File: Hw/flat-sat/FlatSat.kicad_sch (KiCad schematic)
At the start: 81 parts, among them J1 Antenna, J2 Antenna, P1 USB_C_Plug_USB2.0, SW1 SW, SW2 SW, U1 AP2112K-3.3, U10 LIS2DH, U2 0900FM15D0039, U3 PE42421, U4 SX1262IMLTRT, U5 W25Q16JV, U6 0900FM15D0039, U7 PE42421, U8 SX1262IMLTRT, U9 RP2040, Y1 32Mhz, Y2 32Mhz, Y3 12MHz

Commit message: feat(Hw):Update_sch
Pending review
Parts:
- removed SW1, SW2: SW, CatSniffer:TS1088R02026, symbol CatSniffer-rescue:SW_Push-Switch-CatStick-rescue-CatSniffer-rescue
- added J3: Serial, symbol Connector:Conn_01x04_Pin
- added J4: SWD, symbol Connector:Conn_01x04_Pin
- U1: value AP2112K-3.3 -> TLV75733PDBVR; LCSC# (none) -> C485517; Mouser# 865-XC6210B332MR-G -> (none); manf# XC6210B332MR-G -> TLV75733PDBVR; provedor Mouser -> LCSC
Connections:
- net CIPO is gone; now on net R0_CIPO: U9.27 (GPIO16)
- net COPI is gone; now on net R0_COPI: U9.30 (GPIO19)
- net NSS is gone; now on net R0_NSS: U9.28 (GPIO17)
- net R0_DIO22 is gone; now on net DIO2: JP1.1 (A)
- net R1_DIO22 is gone; now on net DIO23: JP2.1 (A)
- net SCK is gone; now on net R0_SCK: U9.29 (GPIO18)
- net +3V3: now also J3.4 (Pin_4), J4.4 (Pin_4)
- net GND: now also J3.1 (Pin_1), J4.1 (Pin_1)
- net LED1: now also U9.16 (GPIO13); no longer U9.40 (GPIO28_ADC2)
- net LED2: now also U9.17 (GPIO14); no longer U9.39 (GPIO27_ADC1)
- net LED3: now also U9.18 (GPIO15); no longer U9.38 (GPIO26_ADC0)
- net R0_ANT_SW: now also U9.40 (GPIO28_ADC2)
- net R0_BUSY: now also U9.9 (GPIO7)
- net R0_DIO1: now also U9.5 (GPIO3)
- net R0_DIO2: now also U9.6 (GPIO4)
- net R0_DIO3: now also U9.7 (GPIO5)
- net R0_RST: now also U9.8 (GPIO6)
- net R1_ANT_SW: now also U9.41 (GPIO29_ADC3)
- net R1_BUSY: now also U9.15 (GPIO12)
- net R1_CIPO: now also U9.36 (GPIO24)
- net R1_COPI: now also U9.39 (GPIO27_ADC1)
- net R1_DIO1: now also U9.11 (GPIO8)
- net R1_DIO2: now also U9.12 (GPIO9)
- net R1_DIO3: now also U9.13 (GPIO10)
- net R1_NSS: now also U9.37 (GPIO25)
- net R1_RST: now also U9.14 (GPIO11)
- net R1_SCK: now also U9.38 (GPIO26_ADC0)
- net SWCLK: now also J4.3 (Pin_3)
- net SCL: now reaches U10.1 (SCL/SPC)
- net SCL: now also U9.32 (GPIO21)
- net SDA: now reaches U10.2 (SDA/SDI)
- net SDA: now also U9.31 (GPIO20)
- net INT1: now reaches U10.6 (INT1)
- net INT1: now also U9.34 (GPIO22)
- net TXD: now reaches U9.2 (GPIO0)
- net TXD: now also J3.3 (Pin_3)
- net RXD: now reaches U9.3 (GPIO1)
- net RXD: now also J3.2 (Pin_2)
- net DIO23: now reaches U9.35 (GPIO23)
- net DIO2: now reaches U9.4 (GPIO2)
- new net SWDIO: J4.2 (Pin_2)
- no-connect marks 3 -> 5
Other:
- moved on the sheet: BOOT1, C6, C7, JP1, JP2, R1, R2, RESET1, U1, U10

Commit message: fet(Hw):Init_floorplan_Update_LCSC#
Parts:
- removed D2, D3: LED, LED_SMD:LED_0603_1608Metric_Pad1.05x0.95mm_HandSolder, symbol CatSniffer-rescue:LED_Small-Device-CatStick-rescue-CatSniffer-rescue
- removed R11, R12: 330, Resistor_SMD:R_0603_1608Metric, symbol CatSniffer-rescue:R_Small-Device-CatStick-rescue-CatSniffer-rescue
- added Button1, Button2: SW, CatSniffer:TS1088R02026, symbol CatSniffer-rescue:SW_Push-Switch-CatStick-rescue-CatSniffer-rescue
- added C37: 0.1uF, Capacitor_SMD:C_0402_1005Metric, symbol Device:C_Small
- added R11, R12: 10k, Resistor_SMD:R_0402_1005Metric, symbol Device:R_Small
- BOOT1, RESET1: manf# TS-1088R-02526 -> (none)
- C1, C14, C18, C19, C5, C7, C8: footprint Capacitor_SMD:C_0603_1608Metric -> Capacitor_SMD:C_0402_1005Metric; LCSC# C14663 -> C56392; manf# CC0603KRX7R9BB104 -> (none)
- C10, C12, C21, C23: footprint Capacitor_SMD:C_0603_1608Metric -> Capacitor_SMD:C_0402_1005Metric; LCSC# C1588 -> C710873; manf# CL10B102KB8NNNC -> (none)
- C11, C22: footprint Capacitor_SMD:C_0603_1608Metric -> Capacitor_SMD:C_0402_1005Metric; LCSC# C170149 -> C47339; manf# CL10A474KB8NNNC -> (none)
- C13, C24, C25, C27, C28, C32, C33, C34, C35, C36: LCSC# (none) -> C56392; manf# MSAST105SB7104KFNB25 -> (none)
- C15, C2: footprint Capacitor_SMD:C_0603_1608Metric -> Capacitor_SMD:C_0402_1005Metric; LCSC# C14858 -> C541374; manf# CL10C101JB8NNNC -> (none)
- C16, C17, C3, C4: footprint Capacitor_SMD:C_0603_1608Metric -> Capacitor_SMD:C_0402_1005Metric; LCSC# C162225 -> C1565; manf# GRM1885C1H3R3CA01D -> (none)
- C20, C9: footprint Capacitor_SMD:C_0603_1608Metric -> Capacitor_SMD:C_0402_1005Metric; LCSC# C519486 -> C437519; manf# CC0603FRNPO9BN470 -> (none)
- C26, C31: LCSC# (none) -> C52923; manf# MSRLJ103SB5105MFNA01 -> (none)
- C29, C30: LCSC# (none) -> C424826; manf# GJM1555C1H270FB01D -> (none)
- C6: footprint Capacitor_SMD:C_0603_1608Metric -> Capacitor_SMD:C_0402_1005Metric; LCSC# C108343 -> C52923; manf# 0603F105M500NT -> (none)
- D1: manf# CL10C120JB81PNC -> (none)
- F1: value 0.5A -> 0.75A; footprint Fuse:Fuse_0805_2012Metric_Pad1.15x1.40mm_HandSolder -> Fuse:Fuse_0603_1608Metric_Pad1.05x0.95mm_HandSolder; LCSC# (none) -> C182438; manf# MFU0805FF00500P100 -> (none)
- J1, J2: footprint bast-wan:SMA_EDGE -> FlatSat:SMA_EDGE; manf# KH-SMA-KE8-G -> (none)
- J3, J4: footprint (none) -> Connector_PinHeader_2.54mm:PinHeader_1x04_P2.54mm_Vertical
- L1, L4: manf# VHF160808H9N1JT -> (none)
- L2, L5: manf# SCHF160808H47NJT -> (none)
- L3, L6: manf# SDFL1608T150KTF -> (none)
- P1: footprint Connectors:C393939 -> FlatSat:C393939; manf# KH-TYPE-C-16P -> (none)
- R1, R2: footprint Resistor_SMD:R_0603_1608Metric -> Resistor_SMD:R_0402_1005Metric; LCSC# C319561 -> C25905; manf# AR03DTCX5101 -> (none)
- R10, R8: LCSC# (none) -> C25100; manf# ESR01MZPF27R0 -> (none)
- R13: LCSC# (none) -> C11702; manf# MCS0402MD1001DE000 -> (none)
- R3, R4, R6, R7: footprint Resistor_SMD:R_0603_1608Metric -> Resistor_SMD:R_0402_1005Metric; LCSC# C700506 -> C25076; manf# RT0603DRD07100RL -> (none)
- R5: LCSC# (none) -> C25531; manf# MCS04020D1002BE000 -> (none)
- R9: manf# AR03BTB3300 -> (none)
- U1: manf# TLV75733PDBVR -> (none)
- U2, U6: footprint CatSniffer:0900FM15D0039E -> FlatSat:0900FM15D0039E
- U3, U7: LCSC# - -> C470893
- U4, U8: LCSC# (none) -> C191341
- U5: footprint CatSniffer:W25Q16JVUUIQ -> Package_SON:Winbond_USON-8-2EP_3x4mm_P0.8mm_EP0.2x0.8mm; LCSC# (none) -> C571259
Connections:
- net +3V3: now also C37.1, R11.1, R12.1
- net GND: now also Button1.2, Button2.2, C37.2
- net LED1: now also D1.2 (A)
- net SCL: now also R12.2
- net SDA: now also R11.2
- net LED2 renamed Butt_1
- net Butt_1: now also Button1.1
- net LED3 renamed Butt_2
- net Butt_2: now also Button2.1; no longer D1.2 (A)
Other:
- moved on the sheet: U10

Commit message: feat(Hw):Update_Pcb_And
Pending_some_pins
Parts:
- BOOT1, Button1, Button2, RESET1: footprint CatSniffer:TS1088R02026 -> Button_Switch_SMD:SW_SPST_TL3342
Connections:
- net SWD is gone; now on net SWDIO: U9.25 (SWD)
- net Butt_1: now also U9.15 (GPIO12); no longer U9.17 (GPIO14)
- net Butt_2: now also U9.16 (GPIO13); no longer U9.18 (GPIO15)
- net GND: now also U4.25 (EXP), U8.25 (EXP)
- net LED1: now also U9.18 (GPIO15); no longer U9.16 (GPIO13)
- net R0_BUSY: now also U9.38 (GPIO26_ADC0); no longer U9.9 (GPIO7)
- net R0_DIO2: now also U9.36 (GPIO24); no longer U9.6 (GPIO4)
- net R0_DIO3: now also U9.37 (GPIO25); no longer U9.7 (GPIO5)
- net R0_RST: now also U9.39 (GPIO27_ADC1); no longer U9.8 (GPIO6)
- net R1_BUSY: now also U9.17 (GPIO14); no longer U9.15 (GPIO12)
- net R1_CIPO: now also U9.6 (GPIO4); no longer U9.36 (GPIO24)
- net R1_COPI: now also U9.9 (GPIO7); no longer U9.39 (GPIO27_ADC1)
- net R1_NSS: now also U9.7 (GPIO5); no longer U9.37 (GPIO25)
- net R1_SCK: now also U9.8 (GPIO6); no longer U9.38 (GPIO26_ADC0)
- net RXD: now also J3.3 (Pin_3); no longer J3.2 (Pin_2)
- net TXD: now also J3.2 (Pin_2); no longer J3.3 (Pin_3)
- net RD+: now reaches R8.2, U9.47 (USB_DP)
- net RD-: now reaches R10.2, U9.46 (USB_DM)
- no-connect marks 5 -> 3
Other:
- moved on the sheet: C1, C11, C19, C20, C22, C8, C9, L2, L3, L5, L6, U4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

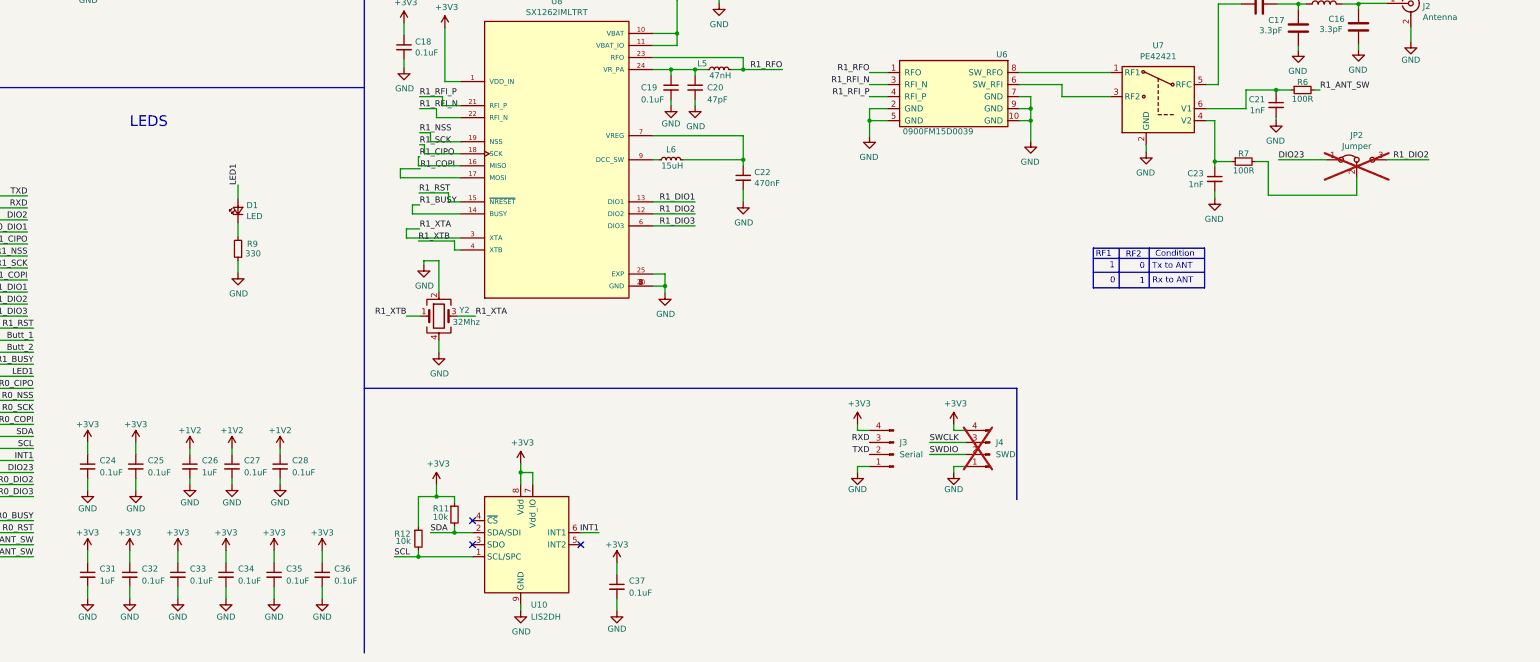
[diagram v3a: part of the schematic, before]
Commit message: feat(Hw):Mounting_Holes_Added
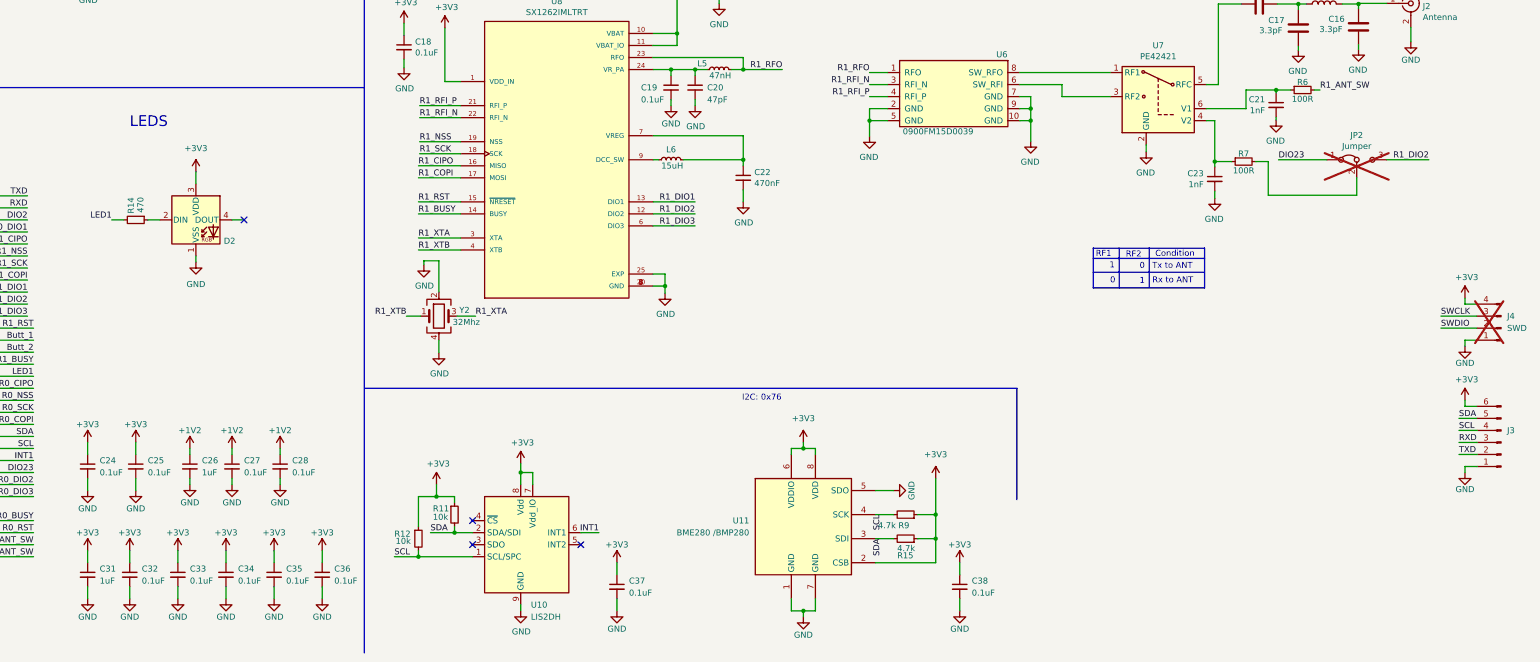
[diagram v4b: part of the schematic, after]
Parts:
- removed D1: LED, LED_SMD:LED_0603_1608Metric_Pad1.05x0.95mm_HandSolder, symbol CatSniffer-rescue:LED_Small-Device-CatStick-rescue-CatSniffer-rescue
- removed J3: Serial, Connector_PinHeader_2.54mm:PinHeader_1x04_P2.54mm_Vertical, symbol Connector:Conn_01x04_Pin
- removed R9: 330, Resistor_SMD:R_0603_1608Metric, symbol CatSniffer-rescue:R_Small-Device-CatStick-rescue-CatSniffer-rescue
- added C38: 0.1uF, Capacitor_SMD:C_0402_1005Metric, symbol Device:C_Small
- added D2: SK6812MINI, Library:SK6812MINI-HS, symbol LED:SK6812MINI
- added J3: periphs, Connector_PinHeader_2.54mm:PinHeader_1x06_P2.54mm_Vertical, symbol Connector:Conn_01x06_Pin
- added R14: 470, Resistor_SMD:R_0402_1005Metric, symbol CatSniffer-rescue:R_Small-Device-CatStick-rescue-CatSniffer-rescue
- added R15, R9: 4.7k, Resistor_SMD:R_0402_1005Metric, symbol Device:R_Small
- added U11: BME280 /BMP280, Package_LGA:Bosch_LGA-8_2.5x2.5mm_P0.65mm_ClockwisePinNumbering, symbol Sensor:BME280
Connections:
- net +3V3: now also C38.1, D2.3 (VDD), J3.6 (Pin_6), R15.1, R9.1, U11.2 (CSB), U11.6 (VDDIO), U11.8 (VDD)
- net GND: now also C38.2, D2.1 (VSS), J3.1 (Pin_1), U11.1 (GND), U11.5 (SDO), U11.7 (GND)
- net LED1: now also R14.2
- net RXD: now also J3.3 (Pin_3)
- net SCL: now also J3.4 (Pin_4), R9.2, U11.4 (SCK)
- net SDA: now also J3.5 (Pin_5), R15.2, U11.3 (SDI)
- net TXD: now also J3.2 (Pin_2)
- new net: D2.2 (DIN), R14.1
- no-connect marks 3 -> 4
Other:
- note added: "I2C: 0x76"
- moved on the sheet: J4

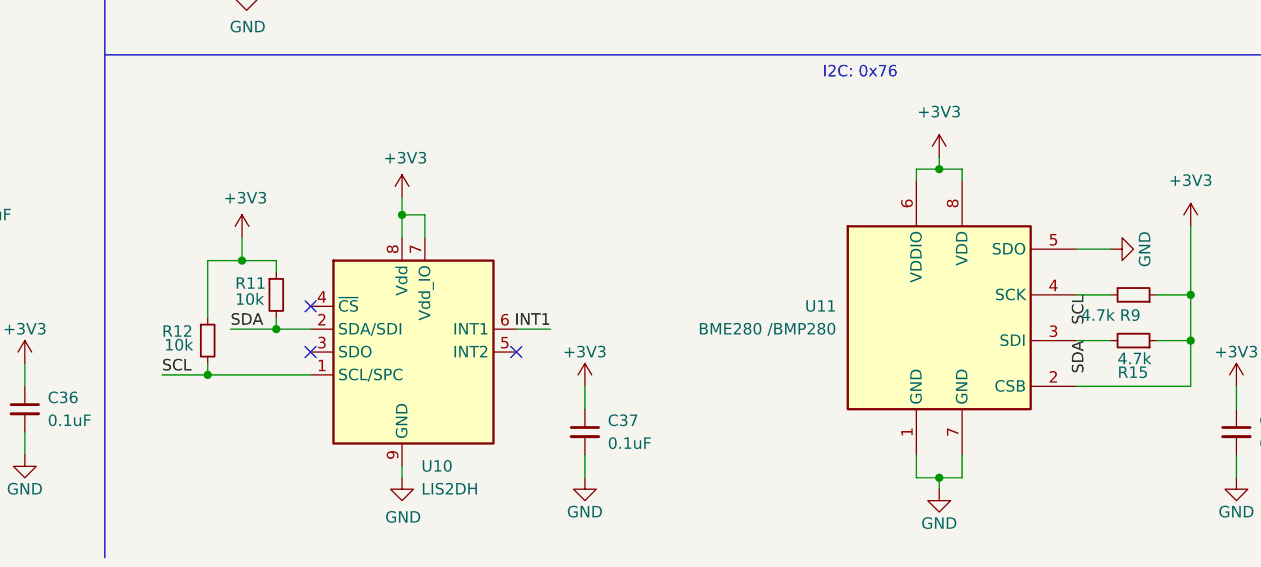
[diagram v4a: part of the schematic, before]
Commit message: feat(Hw):Update_PCB_Change_Buttons
Pending_Check_LIS2DH
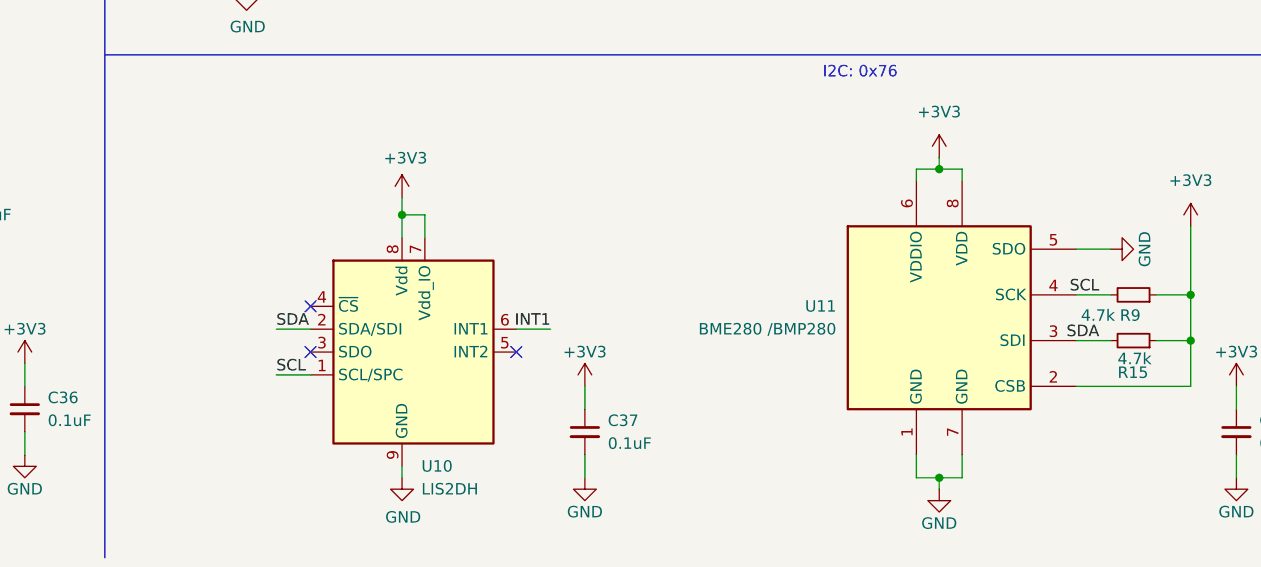
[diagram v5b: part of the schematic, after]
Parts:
- removed R11, R12: 10k, Resistor_SMD:R_0402_1005Metric, symbol Device:R_Small
- BOOT1, Button1, Button2, RESET1: footprint Button_Switch_SMD:SW_SPST_TL3342 -> FlatSat:TS1088R02026
- U10: LCSC# C110926 -> C155670

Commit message: feat(Hw):Update_BoM
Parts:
- C10, C12, C21, C23: LCSC# C710873 -> C335530
- C13, C24, C25, C27, C28, C32, C33, C34, C35, C36, C37, C38: Mouser# 963-MSAST105SB7104KF -> (none)
- C26, C31: Mouser# 963-MSRLJ103SB5105MF -> (none)
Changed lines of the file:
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@@
 			)
 		)
-		(property "LCSC#" "C710873 "
+		(property "LCSC#" "C335530"
 			(at 352.298 63.754 0)
 			(effects
@@
 			)
 		)
-		(property "Mouser#" "963-MSRLJ103SB5105MF"
+		(property "Mouser#" ""
 			(at 137.16 228.6 0)
 			(effects
@@
 			)
 		)
-		(property "Mouser#" "963-MSAST105SB7104KF"
+		(property "Mouser#" ""
 			(at 125.73 228.6 0)
 			(effects
@@
 			)
 		)
-		(property "Mouser#" "963-MSAST105SB7104KF"
+		(property "Mouser#" ""
 			(at 134.62 251.46 0)
 			(effects
@@
 			)
 		)
-		(property "Mouser#" "963-MSRLJ103SB5105MF"
+		(property "Mouser#" ""
 			(at 115.57 251.46 0)
 			(effects
@@
 			)
 		)
-		(property "LCSC#" "C710873 "
+		(property "LCSC#" "C335530"
 			(at 353.568 167.894 0)
 			(effects
@@
 			)
 		)
-		(property "LCSC#" "C710873 "
+		(property "LCSC#" "C335530"
 			(at 366.522 152.273 0)
 			(effects
@@
 			)
 		)
-		(property "Mouser#" "963-MSAST105SB7104KF"
+		(property "Mouser#" ""
 			(at 227.33 254 0)
 			(effects
@@
 			)
 		)
-		(property "Mouser#" "963-MSAST105SB7104KF"
+		(property "Mouser#" ""
 			(at 154.94 251.46 0)
 			(effects
@@
 			)
 		)
-		(property "Mouser#" "963-MSAST105SB7104KF"
+		(property "Mouser#" ""
 			(at 72.39 114.3 0)
 			(effects
@@
 			)
 		)
-		(property "Mouser#" "963-MSAST105SB7104KF"
+		(property "Mouser#" ""
 			(at 165.1 251.46 0)
 			(effects
@@
 			)
 		)
-		(property "Mouser#" "963-MSAST105SB7104KF"
+		(property "Mouser#" ""
 			(at 299.72 254 0)
 			(effects
@@
 			)
 		)
-		(property "Mouser#" "963-MSAST105SB7104KF"
+		(property "Mouser#" ""
 			(at 146.05 228.6 0)
 			(effects
@@
 			)
 		)
-		(property "Mouser#" "963-MSAST105SB7104KF"
+		(property "Mouser#" ""
 			(at 156.21 228.6 0)
 			(effects
@@
 			)
 		)
-		(property "Mouser#" "963-MSAST105SB7104KF"
+		(property "Mouser#" ""
 			(at 144.78 251.46 0)
 			(effects
@@
 			)
 		)
-		(property "Mouser#" "963-MSAST105SB7104KF"
+		(property "Mouser#" ""
 			(at 115.57 228.6 0)
 			(effects
@@
 			)
 		)
-		(property "Mouser#" "963-MSAST105SB7104KF"
+		(property "Mouser#" ""
 			(at 124.46 251.46 0)
 			(effects
@@
 			)
 		)
-		(property "LCSC#" "C710873 "
+		(property "LCSC#" "C335530"
 			(at 365.252 48.133 0)
 			(effects
